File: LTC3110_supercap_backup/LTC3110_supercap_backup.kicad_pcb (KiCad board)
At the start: 2 copper layers, 30 parts, among them M1 2N7002, M2 2N7002, P1 CONN_01X02, P2 CONN_01X02, P3 CONN_01X05, Q1 Q_PNP_BCEC, U1 LTC2935-2-TS8, U2 LTC3110EFE

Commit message: Layout almost complete
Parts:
- U1: footprint TO_SOT_Packages_SMD:SOT-23 -> MRV_SMD_Packages:TSOT-23-8
- moved R6 84.6 mm to (157.2, 142.7)
- moved R12 84.0 mm to (147.8, 140.5), turned to 270 degrees
- moved R13 83.7 mm to (152.2, 139.3), turned to 180 degrees
- moved R8 79.4 mm to (152.1, 134.8), turned to 180 degrees
- moved R5 79.0 mm to (140.3, 139.6), turned to 90 degrees
- moved R11 79.0 mm to (147.8, 135.4), turned to 270 degrees
- moved M1 77.5 mm to (143.1, 138.3)
- moved R9 75.2 mm to (152.2, 137.0)
- moved R2 75.0 mm to (132.4, 139.6), turned to 90 degrees
- moved R10 74.2 mm to (152.1, 141.5), turned to 180 degrees
- moved R7 73.3 mm to (141.0, 129.8), turned to 90 degrees
- moved R3 72.9 mm to (135.0, 139.6), turned to 90 degrees
- moved P2 70.7 mm to (121.1, 111.8), turned to 270 degrees
- moved C4 70.1 mm to (145.0, 135.2), turned to 270 degrees
- moved R4 67.1 mm to (137.9, 139.6), turned to 90 degrees
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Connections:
- C3 pad 1: Net-(C3-Pad1) -> /VCAP
- R12 pad 2: Net-(R12-Pad2) -> V_SYS
- R13 pad 1: Net-(R12-Pad2) -> V_SYS
- R9 pad 2: Net-(R12-Pad2) -> V_SYS
- U2 pad 25: (no net) -> GND
- U2 pad 6: GNDA -> GND
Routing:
- net CAP_OK: track 0.00 -> 75.0 mm, vias 0 -> 2
- net !CHRG: track 0.00 -> 74.8 mm, vias 0 -> 2
- net CAP_LOW: track 0.00 -> 71.9 mm, vias 0 -> 3
- net V_SYS: track 0.00 -> 66.5 mm, vias 0 -> 2
- net /VCAP: track 0.00 -> 65.5 mm, vias 0 -> 1
- net Net-(M1-Pad3): track 0.00 -> 52.4 mm, vias 0 -> 2
- net V_SOLAR: track 0.00 -> 34.6 mm
- net GND: track 0.00 -> 33.9 mm, vias 0 -> 10
- net /RUN: track 0.00 -> 25.8 mm, vias 0 -> 3
- net Net-(C5-Pad2): track 0.00 -> 21.9 mm, vias 0 -> 2
- net Net-(C4-Pad1): track 0.00 -> 18.9 mm
- net /V_MID: track 0.00 -> 18.7 mm
- net /FBVCAP: track 0.00 -> 15.5 mm, vias 0 -> 2
- net /FB: track 0.00 -> 14.3 mm
- net /MODE: track 0.00 -> 10.9 mm, vias 0 -> 2
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- added copper zone on F.Cu, net /VCAP
- added copper zone on F.Cu, net /V_MID
- added copper zone on B.Cu, net GND
- added copper zone on F.Cu, net GND
- added copper zone on F.Cu, net Net-(L1-Pad1)
- added copper zone on F.Cu, net Net-(L1-Pad2)
- added copper zone on F.Cu, net V_SYS
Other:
- board outline added: 95 x 43.7 mm

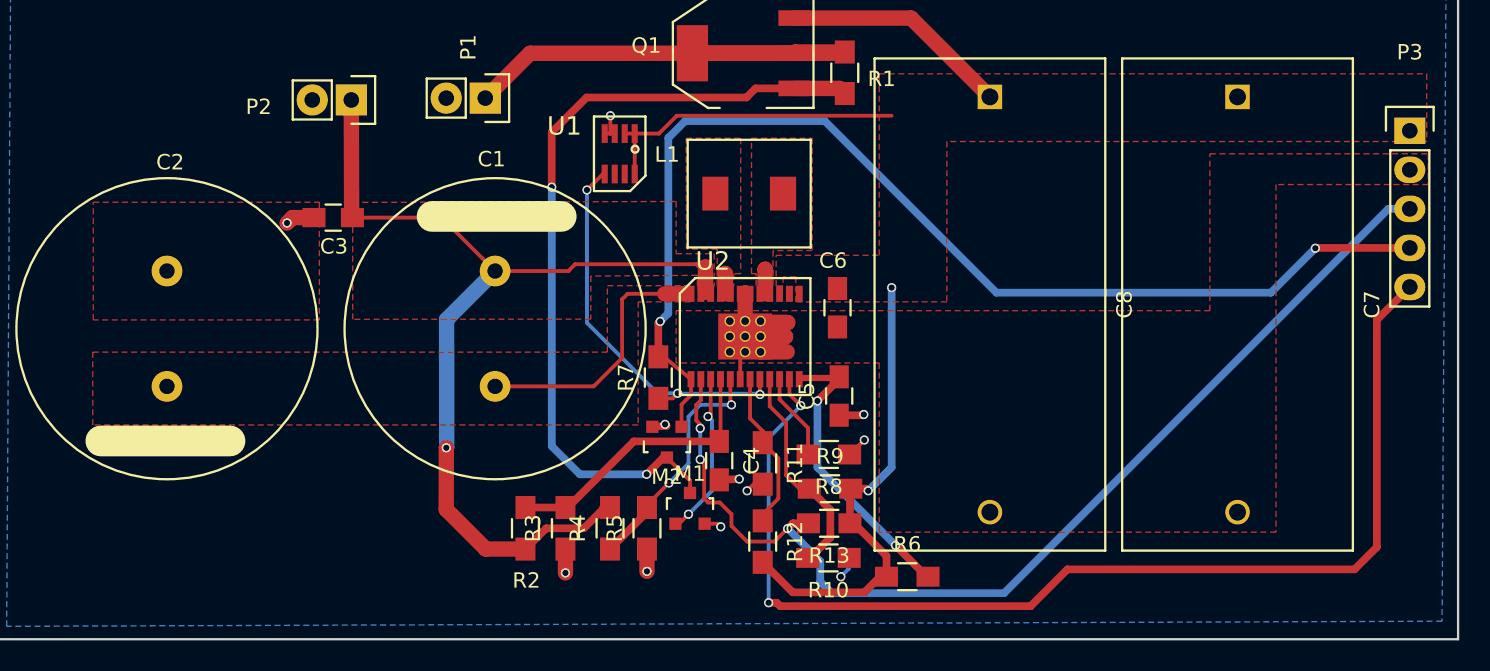
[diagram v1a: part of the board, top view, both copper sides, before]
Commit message: re-routed CAP_OK to avoid major ground plane division
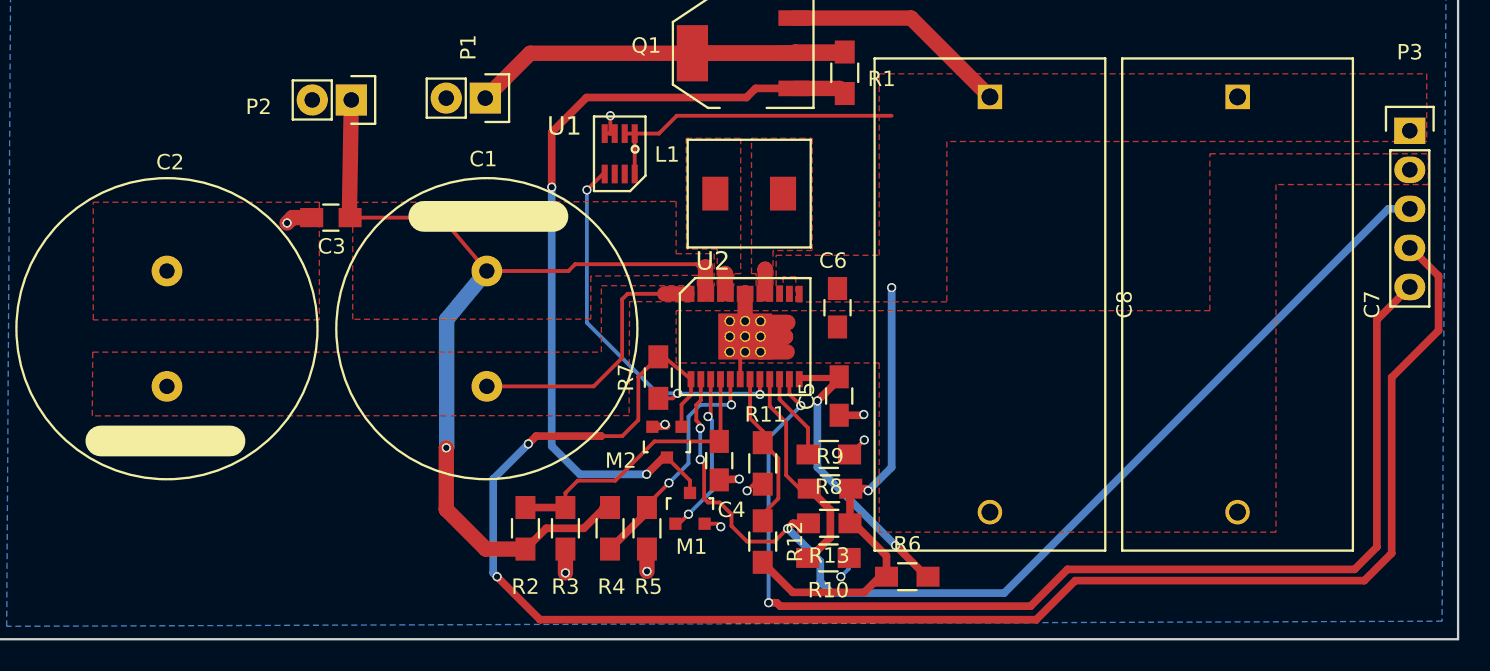
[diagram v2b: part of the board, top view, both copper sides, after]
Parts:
- C1, C2: value CP1 -> 110F
- P1: value CONN_01X02 -> 6v, 150mA solar, ~12 cells
- moved C1 0.54 mm to (129.9, 126.6)
- moved C3 0.15 mm to (119.8, 119.4)
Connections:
- net !CHRG renamed ~CHRG
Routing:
- net CAP_OK: track 75.0 -> 111.3 mm
- net /V_MID: track 18.7 -> 20.2 mm
- net Net-(C4-Pad1): track 18.9 -> 19.6 mm

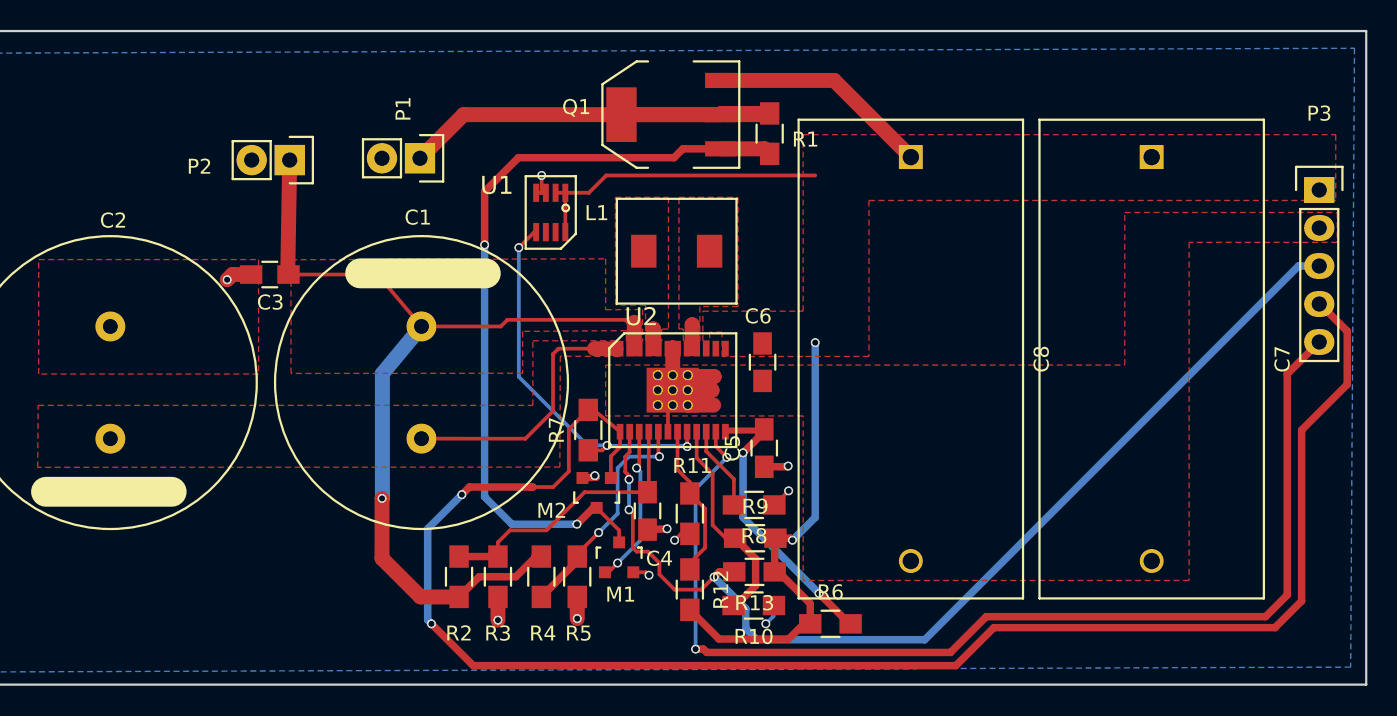
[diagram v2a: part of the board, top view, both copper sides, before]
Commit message: fixed silk screen designator problems and small tweaks to fill areas
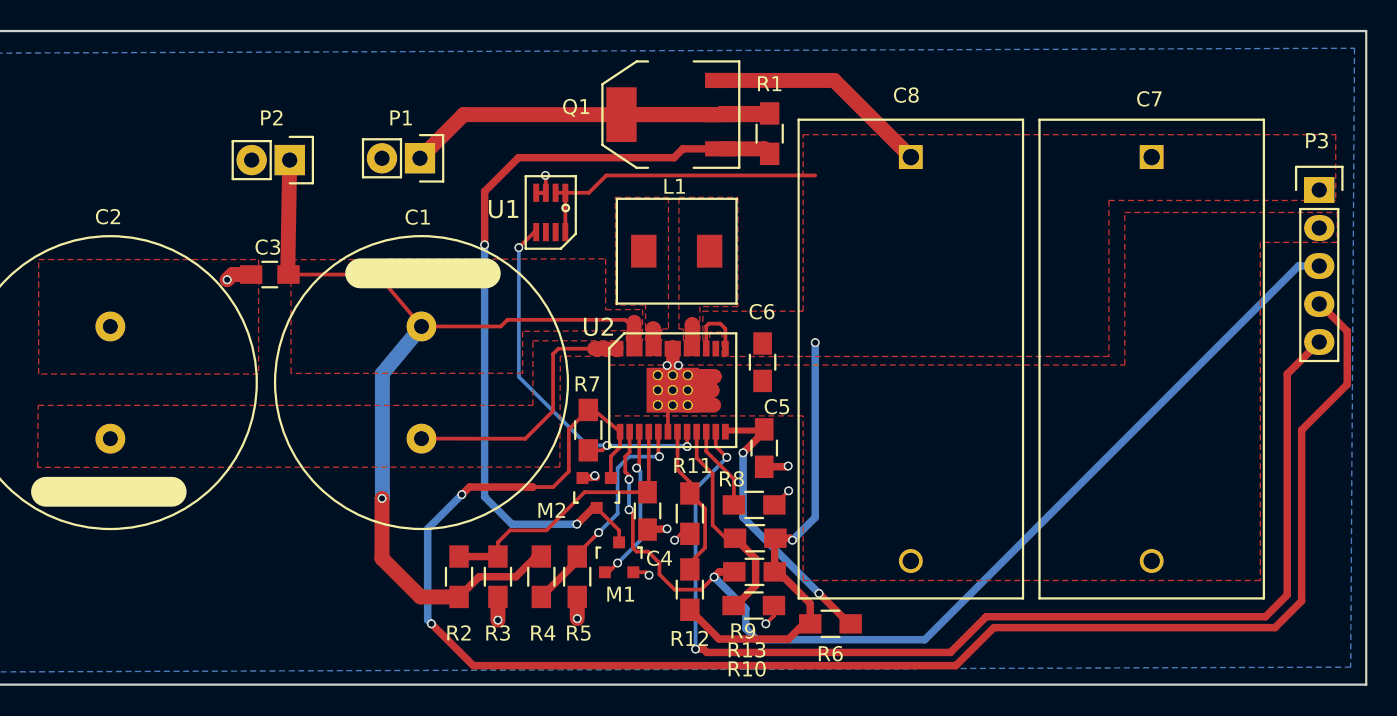
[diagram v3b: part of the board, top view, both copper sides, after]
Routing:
- net GND: track 33.8 -> 45.7 mm, vias 10 -> 13
- net V_SYS: track 66.5 -> 70.8 mm
- net (no net): track 1.48 -> 0.00 mm, vias 1 -> 0
- net /VCAP: track 65.9 -> 66.6 mm

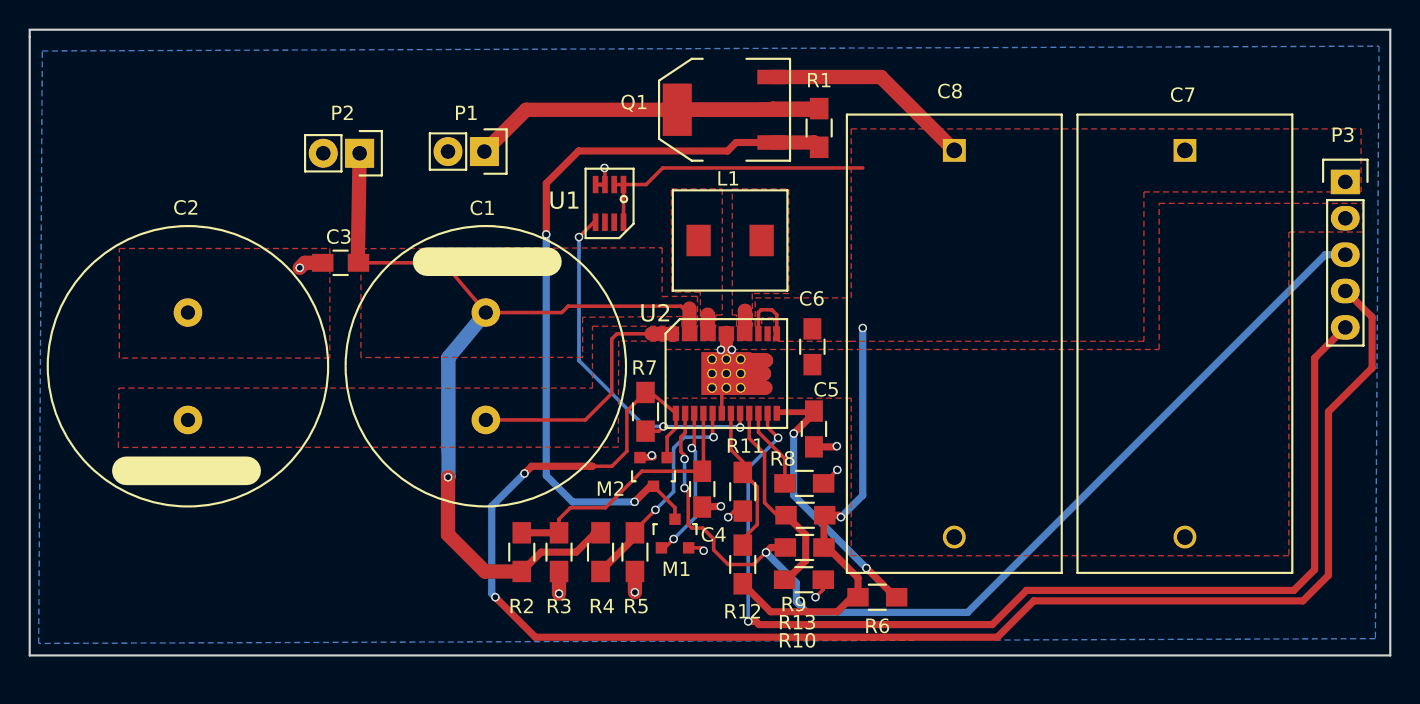
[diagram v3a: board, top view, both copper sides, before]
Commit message: added more silk screen info for debug, board name, etc
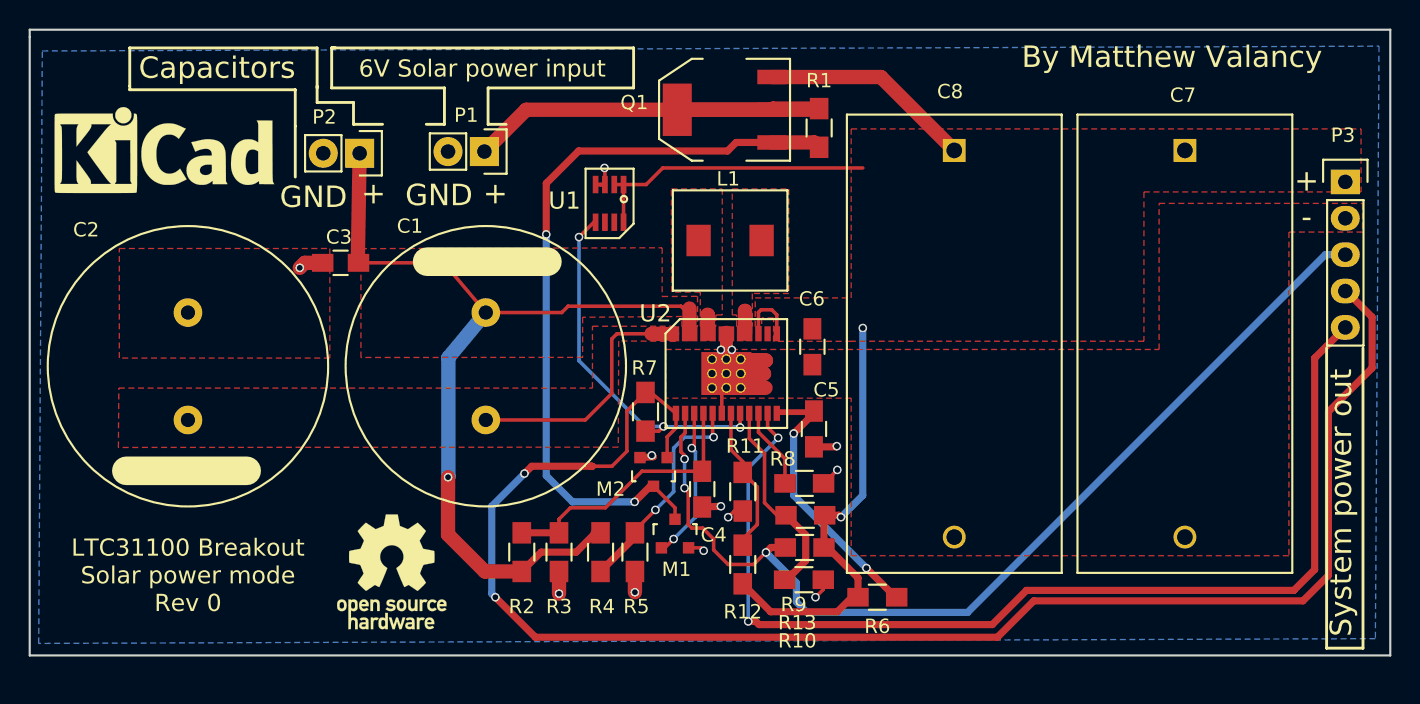
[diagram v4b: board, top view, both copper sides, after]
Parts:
- added REF***: KiCad-Logo_6mm_SilkScreen, Symbols:KiCad-Logo_6mm_SilkScreen, F.Cu at (107.4, 111.5)
- added REF***: OSHW-Logo_7.5x8mm_SilkScreen, Symbols:OSHW-Logo_7.5x8mm_SilkScreen, F.Cu at (123.3, 141.0)
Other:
- board text added: "+"
- board text added: "-"
- board text added: "6V Solar power input"
- board text added: "By Matthew Valancy"
- board text added: "CAP_LOW"
- board text added: "CAP_OK"
- board text added: "Capacitors"
- board text added: "GND"
- board text added: "LTC31100 Breakout Solar power mode Rev 0"
- board text added: "System power out"
- board text added: "~CHRG"
